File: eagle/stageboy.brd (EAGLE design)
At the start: 120 x 75 mm, 35 parts, among them IC1 MEGA8-P, IC2 7805TV, Q1 16MHz, X1 MIDI IN, X2 MIDI OUT, X6 GBIO

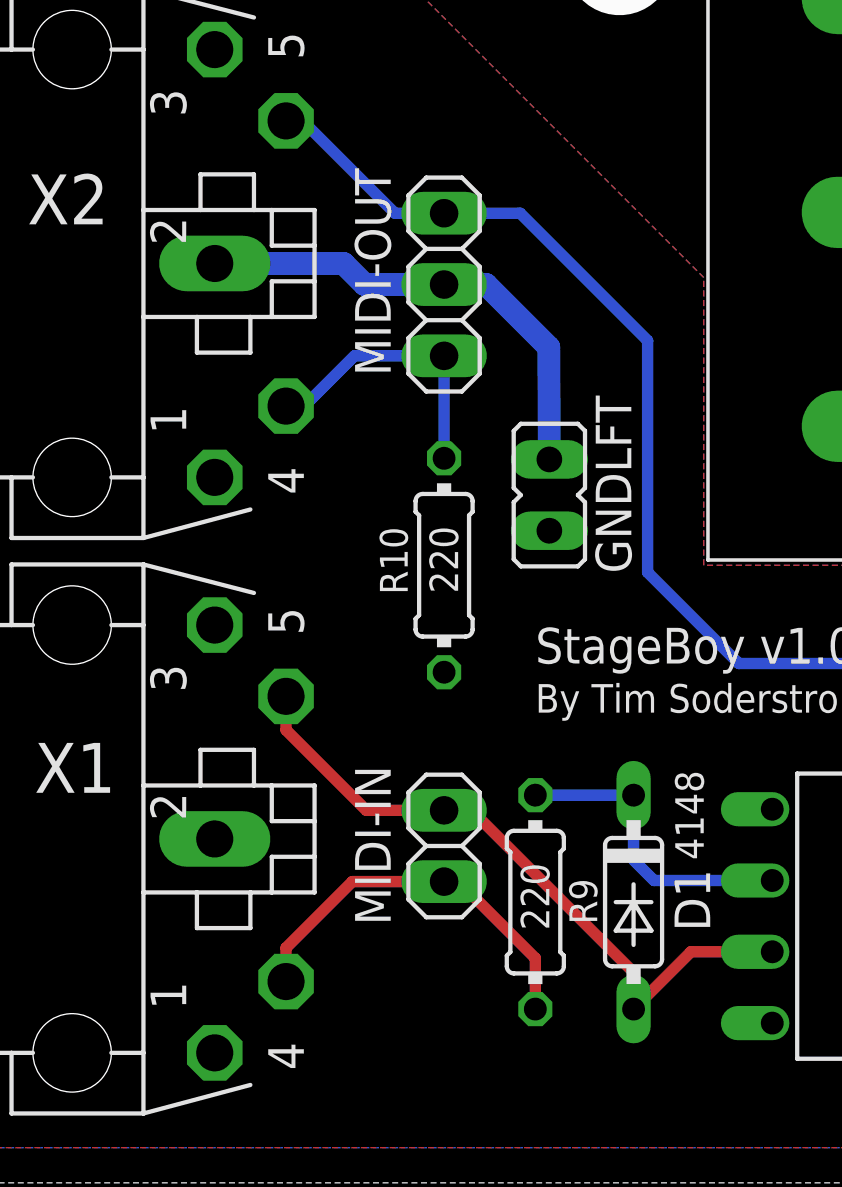
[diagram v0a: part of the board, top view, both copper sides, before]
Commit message: MIDI-IN header was a bit tight
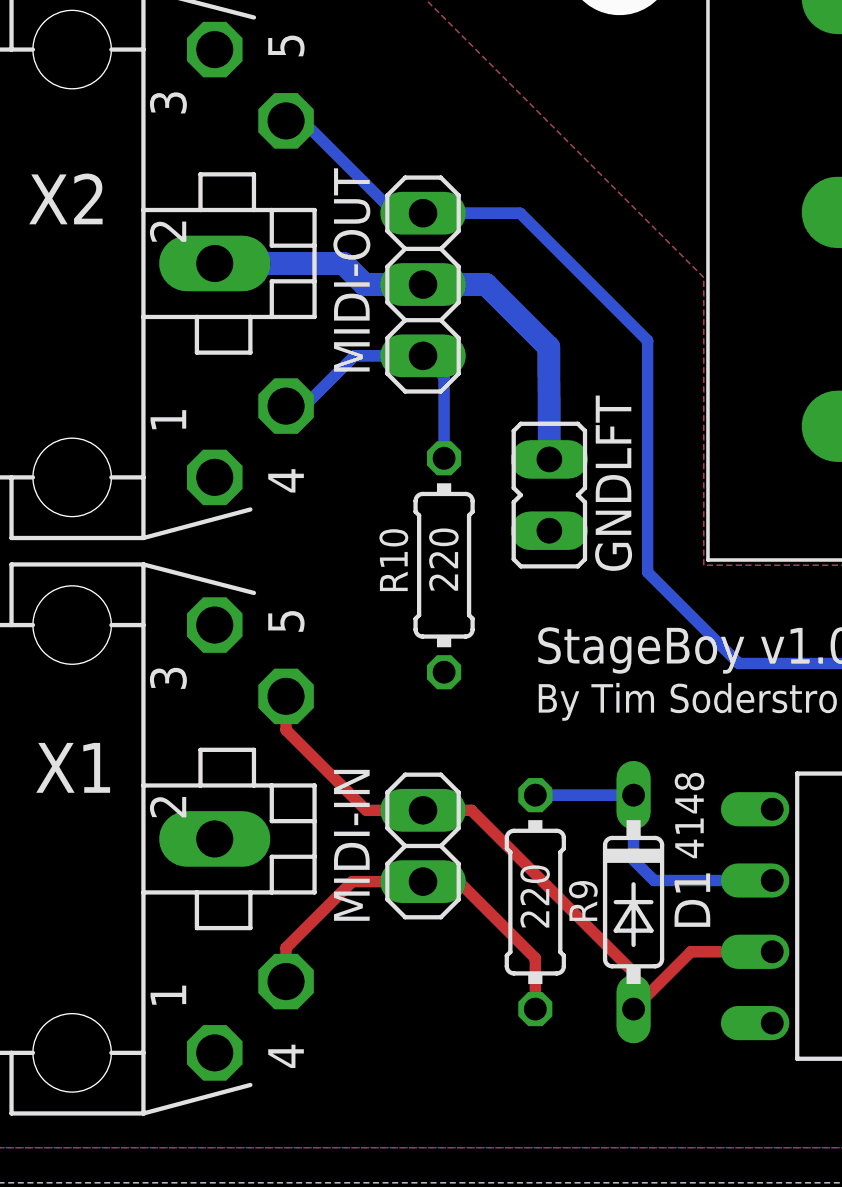
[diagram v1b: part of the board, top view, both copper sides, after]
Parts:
- moved MIDI-IN 0.75 mm to (20.2, 14.0)
- moved MIDI-OUT 0.75 mm to (20.2, 34.0)
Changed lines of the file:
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@@
 <attribute name="VALUE" x="103.421" y="44.21" size="1.27" layer="27" ratio="10" rot="R90"/>
 </element>
-<element name="MIDI-OUT" library="pinhead" package="1X03" value="MIDI OUT" x="21" y="34" smashed="yes" rot="R270">
-<attribute name="NAME" x="17.8288" y="38.1362" size="1.27" layer="25" ratio="10" rot="R270"/>
-<attribute name="VALUE" x="17.825" y="37.81" size="1.27" layer="27" rot="R270"/>
+<element name="MIDI-OUT" library="pinhead" package="1X03" value="MIDI OUT" x="20.25" y="34" smashed="yes" rot="R270">
+<attribute name="NAME" x="17.0788" y="38.1362" size="1.27" layer="25" ratio="10" rot="R270"/>
+<attribute name="VALUE" x="17.075" y="37.81" size="1.27" layer="27" rot="R270"/>
 </element>
 <element name="X2" library="con-hirschmann" package="MAB5SH" value="MIDI OUT" x="7.75" y="34.75" smashed="yes" rot="R270">
@@
 <attribute name="VALUE" x="7.75" y="39.83" size="1.778" layer="27" ratio="10" rot="R270"/>
 </element>
-<element name="MIDI-IN" library="pinhead" package="1X02" value="MIDI IN" x="21" y="14" smashed="yes" rot="R270">
-<attribute name="NAME" x="17.8288" y="16.8662" size="1.27" layer="25" ratio="10" rot="R270"/>
-<attribute name="VALUE" x="17.825" y="16.54" size="1.27" layer="27" rot="R270"/>
+<element name="MIDI-IN" library="pinhead" package="1X02" value="MIDI IN" x="20.25" y="14" smashed="yes" rot="R270">
+<attribute name="NAME" x="17.0788" y="16.8662" size="1.27" layer="25" ratio="10" rot="R270"/>
+<attribute name="VALUE" x="17.075" y="16.54" size="1.27" layer="27" rot="R270"/>
 </element>
 <element name="C6" library="resistor" package="E2,5-5" value="22uF" x="54.25" y="15.25" smashed="yes">
@@
 <contactref element="X1" pad="5"/>
 <contactref element="MIDI-IN" pad="1"/>
-<wire x1="21" y1="15.27" x2="18.23" y2="15.27" width="0.4064" layer="1"/>
+<wire x1="20.25" y1="15.27" x2="18.23" y2="15.27" width="0.4064" layer="1"/>
 <wire x1="18.23" y1="15.27" x2="15.37" y2="18.13" width="0.4064" layer="1"/>
 <wire x1="15.37" y1="19.33" x2="15.37" y2="18.13" width="0.4064" layer="1"/>
-<wire x1="21" y1="15.27" x2="21.98" y2="15.27" width="0.4064" layer="1"/>
+<wire x1="20.25" y1="15.27" x2="21.98" y2="15.27" width="0.4064" layer="1"/>
 <wire x1="21.98" y1="15.27" x2="27.75" y2="9.5" width="0.4064" layer="1"/>
 <wire x1="27.75" y1="9.5" x2="27.75" y2="8.19" width="0.4064" layer="1"/>
@@
 <contactref element="MIDI-IN" pad="2"/>
 <contactref element="X1" pad="4"/>
-<wire x1="21" y1="12.73" x2="17.73" y2="12.73" width="0.4064" layer="1"/>
+<wire x1="20.25" y1="12.73" x2="17.73" y2="12.73" width="0.4064" layer="1"/>
 <wire x1="17.73" y1="12.73" x2="15.37" y2="10.37" width="0.4064" layer="1"/>
 <wire x1="15.37" y1="9.17" x2="15.37" y2="10.37" width="0.4064" layer="1"/>
 <wire x1="24.25" y1="8.19" x2="24.25" y2="10" width="0.4064" layer="1"/>
 <wire x1="24.25" y1="10" x2="21.52" y2="12.73" width="0.4064" layer="1"/>
-<wire x1="21" y1="12.73" x2="21.52" y2="12.73" width="0.4064" layer="1"/>
+<wire x1="20.25" y1="12.73" x2="21.52" y2="12.73" width="0.4064" layer="1"/>
 </signal>
 <signal name="N$17">
@@
 <wire x1="71.75" y1="23.25" x2="71.75" y2="38.5" width="0.4064" layer="16"/>
 <wire x1="71.75" y1="38.5" x2="77.93" y2="44.68" width="0.4064" layer="16"/>
-<wire x1="21" y1="36.54" x2="23.71" y2="36.54" width="0.4064" layer="16"/>
+<wire x1="20.25" y1="36.54" x2="23.71" y2="36.54" width="0.4064" layer="16"/>
 <wire x1="23.71" y1="36.54" x2="28.25" y2="32" width="0.4064" layer="16"/>
 <wire x1="28.25" y1="32" x2="28.25" y2="23.75" width="0.4064" layer="16"/>
-<wire x1="21" y1="36.54" x2="19.25" y2="36.54" width="0.4064" layer="16"/>
+<wire x1="20.25" y1="36.54" x2="19.25" y2="36.54" width="0.4064" layer="16"/>
 <wire x1="15.37" y1="39.83" x2="15.96" y2="39.83" width="0.4064" layer="16"/>
 <wire x1="15.96" y1="39.83" x2="19.25" y2="36.54" width="0.4064" layer="16"/>
@@
 <contactref element="X2" pad="4"/>
 <contactref element="R10" pad="2"/>
-<wire x1="21" y1="31.46" x2="17.81" y2="31.46" width="0.4064" layer="16"/>
-<wire x1="21" y1="27.81" x2="21" y2="31.46" width="0.4064" layer="16"/>
+<wire x1="20.25" y1="31.46" x2="17.81" y2="31.46" width="0.4064" layer="16"/>
 <wire x1="15.37" y1="29.67" x2="16.02" y2="29.67" width="0.4064" layer="16"/>
 <wire x1="16.02" y1="29.67" x2="17.81" y2="31.46" width="0.4064" layer="16"/>
+<wire x1="21" y1="27.81" x2="21" y2="30.71" width="0.4064" layer="16"/>
+<wire x1="21" y1="30.71" x2="20.25" y2="31.46" width="0.4064" layer="16"/>
 </signal>
 <signal name="N$23">
@@
 <contactref element="X2" pad="2"/>
 <contactref element="GNDLFT" pad="1"/>
-<wire x1="21" y1="34" x2="18.17" y2="34" width="0.8128" layer="16"/>
+<wire x1="20.25" y1="34" x2="18.17" y2="34" width="0.8128" layer="16"/>
 <wire x1="24.75" y1="27.77" x2="24.73" y2="31.77" width="0.8128" layer="16"/>
 <wire x1="24.73" y1="31.77" x2="22.5" y2="34" width="0.8128" layer="16"/>
-<wire x1="22.5" y1="34" x2="21" y2="34" width="0.8128" layer="16"/>
+<wire x1="22.5" y1="34" x2="20.25" y2="34" width="0.8128" layer="16"/>
 <wire x1="12.83" y1="34.75" x2="17.42" y2="34.75" width="0.8128" layer="16"/>
 <wire x1="17.42" y1="34.75" x2="18.17" y2="34" width="0.8128" layer="16"/>
